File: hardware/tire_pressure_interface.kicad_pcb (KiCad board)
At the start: 2 copper layers, 60 x 40 mm, 4 parts

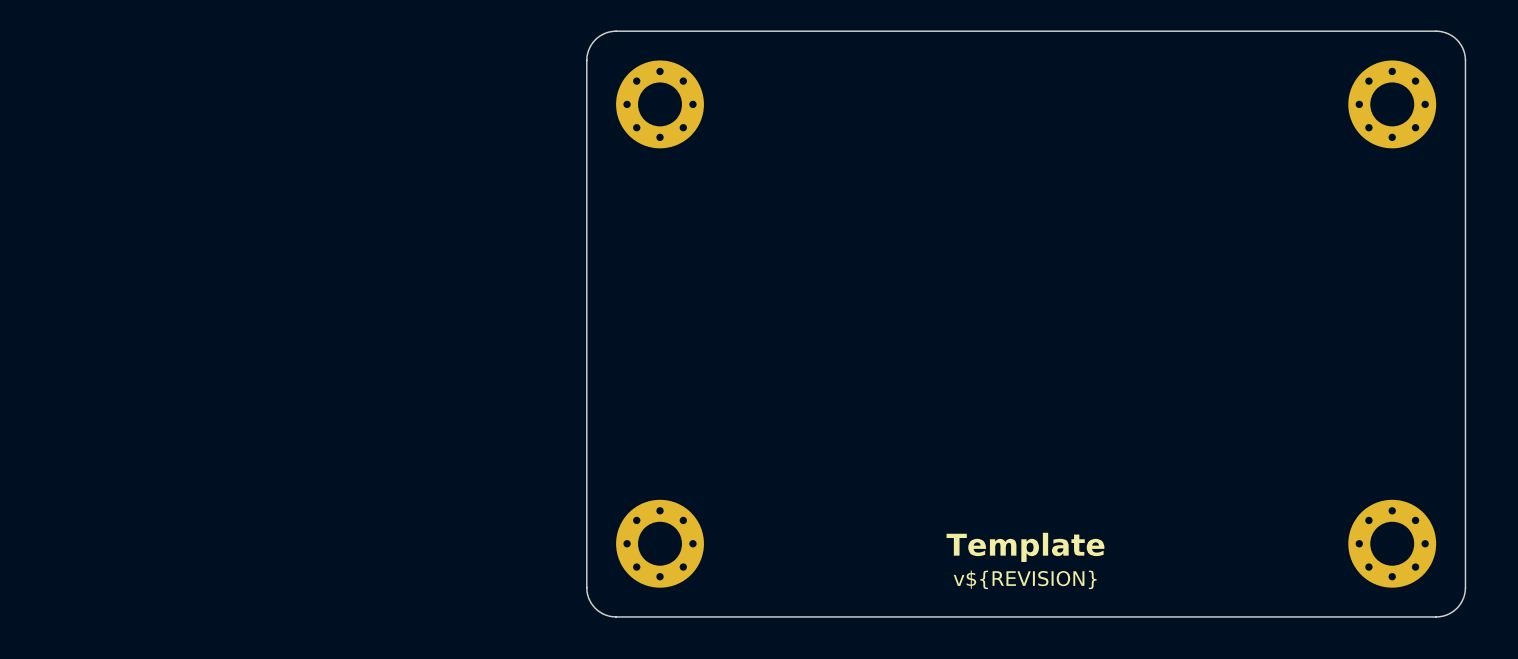
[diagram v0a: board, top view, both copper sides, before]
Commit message: initial component placement
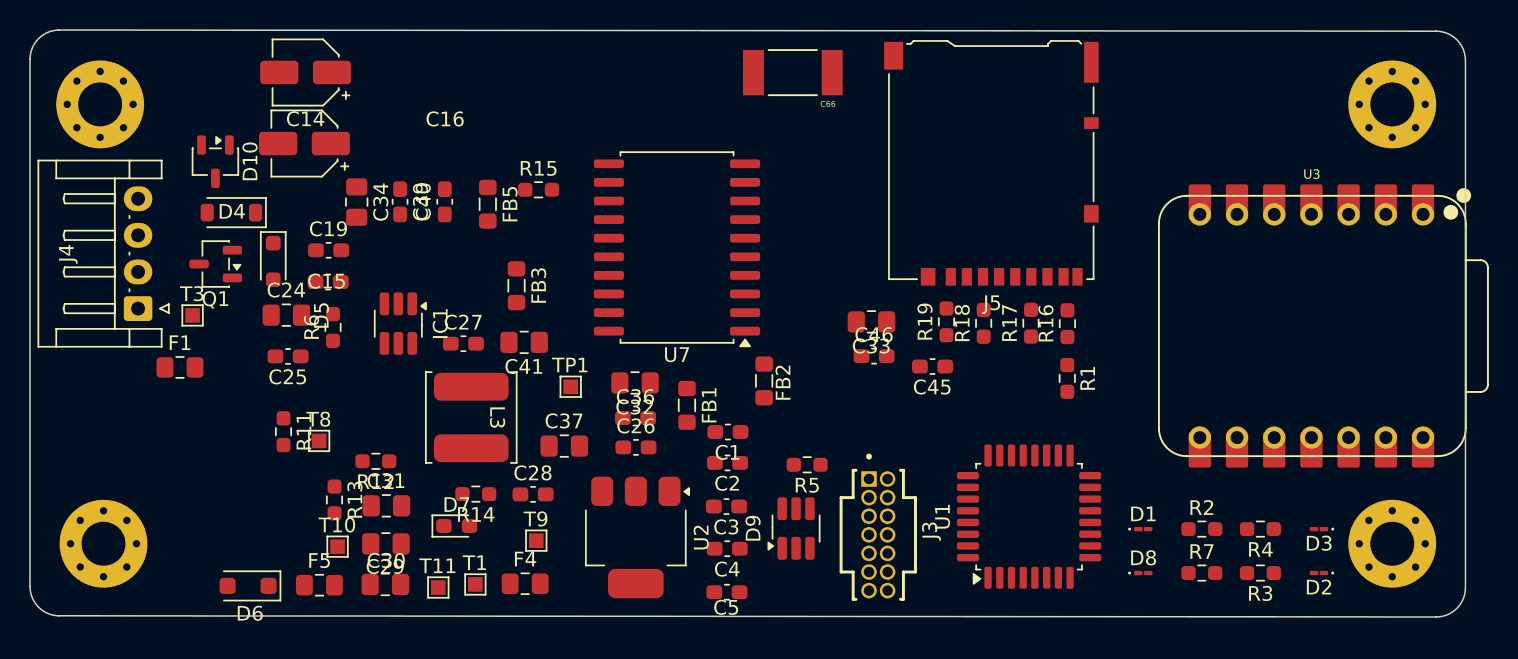
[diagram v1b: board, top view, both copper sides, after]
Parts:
- added C1: 10u, Capacitor_SMD:C_0603_1608Metric_Pad1.08x0.95mm_HandSolder, F.Cu at (125.6, 103.4)
- added C14: 22u, Capacitor_SMD:CP_Elec_4x5.8, F.Cu at (96.8, 78.8)
- added C15: 10u, Capacitor_SMD:C_0603_1608Metric_Pad1.08x0.95mm_HandSolder, F.Cu at (98.3, 93.1)
- added C16: 22u, Capacitor_SMD:CP_Elec_4x5.8, F.Cu at (96.7, 83.7)
- added C19: 10u, Capacitor_SMD:C_0603_1608Metric_Pad1.08x0.95mm_HandSolder, F.Cu at (98.4, 91.0)
- added C2: 4u7, Capacitor_SMD:C_0603_1608Metric_Pad1.08x0.95mm_HandSolder, F.Cu at (125.6, 105.5)
- added C24: 22u, Capacitor_SMD:C_0805_2012Metric_Pad1.18x1.45mm_HandSolder, F.Cu at (95.5, 95.4)
- added C25: 100n, Capacitor_SMD:C_0603_1608Metric_Pad1.08x0.95mm_HandSolder, F.Cu at (95.6, 98.2)
- added C26: 100n, Capacitor_SMD:C_0603_1608Metric_Pad1.08x0.95mm_HandSolder, F.Cu at (119.4, 104.4)
- added C27: 100n, Capacitor_SMD:C_0603_1608Metric_Pad1.08x0.95mm_HandSolder, F.Cu at (107.6, 97.3)
- added C28: 100n, Capacitor_SMD:C_0603_1608Metric_Pad1.08x0.95mm_HandSolder, F.Cu at (112.3, 107.6)
- added C29: 22u, Capacitor_SMD:C_0805_2012Metric_Pad1.18x1.45mm_HandSolder, F.Cu at (102.3, 111.0)
- added C3: 4u7, Capacitor_SMD:C_0603_1608Metric_Pad1.08x0.95mm_HandSolder, F.Cu at (125.5, 108.5)
- added C30: 22u, Capacitor_SMD:C_0805_2012Metric_Pad1.18x1.45mm_HandSolder, F.Cu at (102.2, 113.8)
- added C31: 22u, Capacitor_SMD:C_0805_2012Metric_Pad1.18x1.45mm_HandSolder, F.Cu at (102.3, 108.4)
- added C32: 47u, Capacitor_SMD:C_0805_2012Metric_Pad1.18x1.45mm_HandSolder, F.Cu at (119.3, 100.0)
- added C33: 47u, Capacitor_SMD:C_0805_2012Metric_Pad1.18x1.45mm_HandSolder, F.Cu at (135.4, 95.8)
- added C34: 47u, Capacitor_SMD:C_0805_2012Metric_Pad1.18x1.45mm_HandSolder, F.Cu at (100.3, 87.7)
- added C36: 10u, Capacitor_SMD:C_0603_1608Metric_Pad1.08x0.95mm_HandSolder, F.Cu at (119.3, 102.4)
- added C37: 22u, Capacitor_SMD:C_0805_2012Metric_Pad1.18x1.45mm_HandSolder, F.Cu at (114.5, 104.3)
- added C39: 100n, Capacitor_SMD:C_0603_1608Metric_Pad1.08x0.95mm_HandSolder, F.Cu at (103.2, 87.7)
- added C4: 100n, Capacitor_SMD:C_0603_1608Metric_Pad1.08x0.95mm_HandSolder, F.Cu at (125.6, 111.3)
- added C40: 10n, Capacitor_SMD:C_0603_1608Metric_Pad1.08x0.95mm_HandSolder, F.Cu at (106.3, 87.7)
- added C41: 47u, Capacitor_SMD:C_0805_2012Metric_Pad1.18x1.45mm_HandSolder, F.Cu at (111.7, 97.2)
- added C45: 100n, Capacitor_SMD:C_0603_1608Metric_Pad1.08x0.95mm_HandSolder, F.Cu at (139.6, 98.9)
- added C46: 10n, Capacitor_SMD:C_0603_1608Metric_Pad1.08x0.95mm_HandSolder, F.Cu at (135.6, 98.2)
- added C5: 100n, Capacitor_SMD:C_0603_1608Metric_Pad1.08x0.95mm_HandSolder, F.Cu at (125.6, 114.3)
- added C66: 4.7nF/Y2, XiaoS3:CAPC5727X254N, F.Cu at (130.1, 78.8)
- added D1: LED_Debug, LED_SMD:LED_01005_0402Metric_Pad0.57x0.30mm_HandSolder, F.Cu at (154.0, 110.0)
- added D10: PESD5V0L2BT,215, Package_TO_SOT_SMD:SOT-23-3, F.Cu at (90.6, 84.9)
- added D2: LED_Debug, LED_SMD:LED_01005_0402Metric_Pad0.57x0.30mm_HandSolder, F.Cu at (166.0, 113.0)
- added D3: LED_Debug, LED_SMD:LED_01005_0402Metric_Pad0.57x0.30mm_HandSolder, F.Cu at (166.0, 110.0)
- added D4: 200W/28V, Diode_SMD:D_SOD-123, F.Cu at (91.7, 88.4)
- added D5: 9V1, Diode_SMD:D_SOD-323_HandSoldering, F.Cu at (94.6, 91.7)
- added D6: SKL34, Diode_SMD:D_SOD-123F, F.Cu at (92.9, 113.9)
- added D7: +3V3, LED_SMD:LED_0603_1608Metric_Pad1.05x0.95mm_HandSolder, F.Cu at (107.1, 109.8)
- added D8: LED_Debug, LED_SMD:LED_01005_0402Metric_Pad0.57x0.30mm_HandSolder, F.Cu at (154.0, 113.0)
- added D9: SP0505BAHTG, Package_TO_SOT_SMD:SOT-23-6_Handsoldering, F.Cu at (130.3, 110.0)
- added F1: MFU0805FF00500P500, Fuse:Fuse_0805_2012Metric_Pad1.15x1.40mm_HandSolder, F.Cu at (88.2, 99.0)
- added F4: PICOSMDC050S-2, Fuse:Fuse_0805_2012Metric_Pad1.15x1.40mm_HandSolder, F.Cu at (111.8, 113.7)
- added F5: PICOSMDC050S-2, Fuse:Fuse_0805_2012Metric_Pad1.15x1.40mm_HandSolder, F.Cu at (97.7, 113.8)
- added FB1: 2K@100MHz, Inductor_SMD:L_0805_2012Metric_Pad1.05x1.20mm_HandSolder, F.Cu at (122.8, 101.5)
- added FB2: 2K@100MHz, Inductor_SMD:L_0805_2012Metric_Pad1.05x1.20mm_HandSolder, F.Cu at (128.1, 99.9)
- added FB3: 2K@100MHz, Inductor_SMD:L_0805_2012Metric_Pad1.05x1.20mm_HandSolder, F.Cu at (111.2, 93.4)
- added FB5: 2K@100MHz, Inductor_SMD:L_0805_2012Metric_Pad1.05x1.20mm_HandSolder, F.Cu at (109.2, 87.8)
- added IC1: TPS54202HDDCR, Package_TO_SOT_SMD:SOT-23-6_Handsoldering, F.Cu at (103.1, 96.0)
- added J3: FTSH-107-01-L-D-K, XiaoS3:SAMTEC_FTSH-107-01-L-D-K, F.Cu at (135.9, 110.4)
- added J4: Conn_02x02_Counter_Clockwise, Connector_JST:JST_EH_S4B-EH_1x04_P2.50mm_Horizontal, F.Cu at (85.4, 94.9)
- added J5: Micro_SD_Card_Det1, Connector_Card:microSD_HC_Hirose_DM3AT-SF-PEJM5, F.Cu at (143.6, 85.0)
- added L3: 68u/1A4, Inductor_SMD:L_TDK_VLS6045EX_VLS6045AF, F.Cu at (108.1, 102.4)
- added Q1: SI2347DS-T1-GE3, Package_TO_SOT_SMD:SOT-23-3, F.Cu at (90.7, 91.9)
- added R1: 0, Resistor_SMD:R_0603_1608Metric_Pad0.98x0.95mm_HandSolder, F.Cu at (148.8, 99.7)
- added R11: 510k, Resistor_SMD:R_0603_1608Metric_Pad0.98x0.95mm_HandSolder, F.Cu at (95.3, 103.3)
- added R12: 13k3, Resistor_SMD:R_0603_1608Metric_Pad0.98x0.95mm_HandSolder, F.Cu at (101.6, 105.4)
- added R13: 100k, Resistor_SMD:R_0603_1608Metric_Pad0.98x0.95mm_HandSolder, F.Cu at (98.8, 108.0)
- added R14: 1k, Resistor_SMD:R_0603_1608Metric_Pad0.98x0.95mm_HandSolder, F.Cu at (108.4, 107.6)
- added R15: 100K, Resistor_SMD:R_0603_1608Metric_Pad0.98x0.95mm_HandSolder, F.Cu at (112.7, 86.8)
- added R16: 4k7, Resistor_SMD:R_0603_1608Metric_Pad0.98x0.95mm_HandSolder, F.Cu at (148.8, 96.0)
- added R17: 4k7, Resistor_SMD:R_0603_1608Metric_Pad0.98x0.95mm_HandSolder, F.Cu at (146.3, 95.9)
- added R18: 4k7, Resistor_SMD:R_0603_1608Metric_Pad0.98x0.95mm_HandSolder, F.Cu at (143.1, 96.0)
- added R19: 4k7, Resistor_SMD:R_0603_1608Metric_Pad0.98x0.95mm_HandSolder, F.Cu at (140.6, 95.8)
- added R2: 1k, Resistor_SMD:R_0603_1608Metric_Pad0.98x0.95mm_HandSolder, F.Cu at (158.0, 110.0)
- added R3: 1k, Resistor_SMD:R_0603_1608Metric_Pad0.98x0.95mm_HandSolder, F.Cu at (162.0, 113.0)
- added R4: 1k, Resistor_SMD:R_0603_1608Metric_Pad0.98x0.95mm_HandSolder, F.Cu at (162.0, 110.0)
- added R5: 100k, Resistor_SMD:R_0603_1608Metric_Pad0.98x0.95mm_HandSolder, F.Cu at (131.0, 105.6)
- added R6: 100k, Resistor_SMD:R_0603_1608Metric_Pad0.98x0.95mm_HandSolder, F.Cu at (98.7, 96.2)
- added R7: 1k, Resistor_SMD:R_0603_1608Metric_Pad0.98x0.95mm_HandSolder, F.Cu at (158.0, 113.0)
- added T1: TP_+3V3, TestPoint:TestPoint_Pad_1.0x1.0mm, F.Cu at (108.4, 113.8)
- added T10: TP_+5V, TestPoint:TestPoint_Pad_1.0x1.0mm, F.Cu at (99.0, 111.2)
- added T11: TP_+5V, TestPoint:TestPoint_Pad_1.0x1.0mm, F.Cu at (105.9, 114.0)
- added T3: TP_VCC, TestPoint:TestPoint_Pad_1.0x1.0mm, F.Cu at (89.1, 95.4)
- added T8: TP_VCC, TestPoint:TestPoint_Pad_1.0x1.0mm, F.Cu at (97.7, 104.0)
- added T9: TP_+3V3, TestPoint:TestPoint_Pad_1.0x1.0mm, F.Cu at (112.5, 110.8)
- added TP1: TP_+5V, TestPoint:TestPoint_Pad_1.0x1.0mm, F.Cu at (114.9, 100.3)
- added U1: STM32G0C1KCTxN, Package_QFP:LQFP-32_7x7mm_P0.8mm, F.Cu at (146.2, 109.2)
- added U2: LM1117-3.3, Package_TO_SOT_SMD:SOT-223-3_TabPin2, F.Cu at (119.3, 110.6)
- added U3: XIAO-ESP32-S3-DIP, XiaoS3:XIAO-ESP32-S3-DIP, F.Cu at (165.5, 96.1)
- added U7: ADM3057ExRW, Package_SO:SOIC-20W_7.5x12.8mm_P1.27mm, F.Cu at (122.2, 90.8)
- moved REF** 38.2 mm to (82.8, 81.0)
- moved REF** 38.0 mm to (83.0, 111.0)
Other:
- board size 60 x 40 mm -> 98 x 40.1 mm
- board text removed: "Template"
- board text removed: "v${REVISION}"
